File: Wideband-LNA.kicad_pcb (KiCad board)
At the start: 4 copper layers, 18.8 x 18.8 mm, 32 parts, among them J1 RF-IN, J2 RF-OUT, J3 USB_C_Receptacle_USB2.0_16P, U1 PGA-103, U2 AP2127K-ADJ

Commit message: After the fab and assy, components error fixes
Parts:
- added D2: 4v8, LED_SMD:LED_0402_1005Metric, F.Cu at (130.6, 95.4)
- added R10: 0, Resistor_SMD:R_0402_1005Metric, F.Cu at (110.6, 95.1)
- R1: value 10 -> 1K
- moved R1 10.9 mm to (121.4, 94.9)
- moved D1 1.36 mm to (116.9, 96.2)
- moved C9 0.36 mm to (117.1, 97.5)
- moved C3 0.13 mm to (112.9, 96.0)
- moved C1 0.12 mm to (112.9, 98.0)
- moved L2 0.11 mm to (112.9, 97.0)
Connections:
- R1 pad 2: Net-(C3-Pad1) -> Net-(D2-A)
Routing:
- net /5V: track 17.7 -> 19.3 mm
- net GND: track 15.7 -> 16.2 mm, vias 69 -> 68

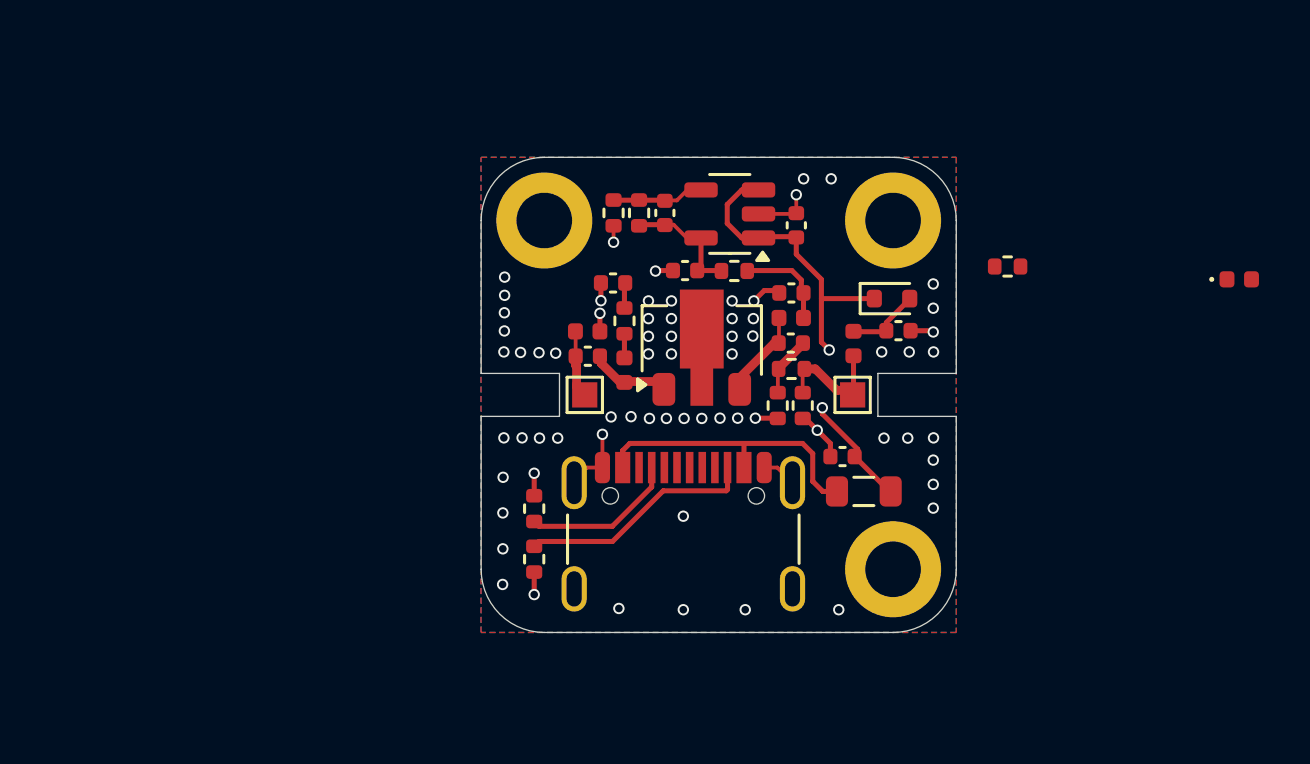
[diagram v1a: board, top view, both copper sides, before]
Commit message: Relayout for 25x25x50 extruded aluminum enclosure Axial coax connectors Isolation of LNA input and output Extensive shielding vias around RF traces
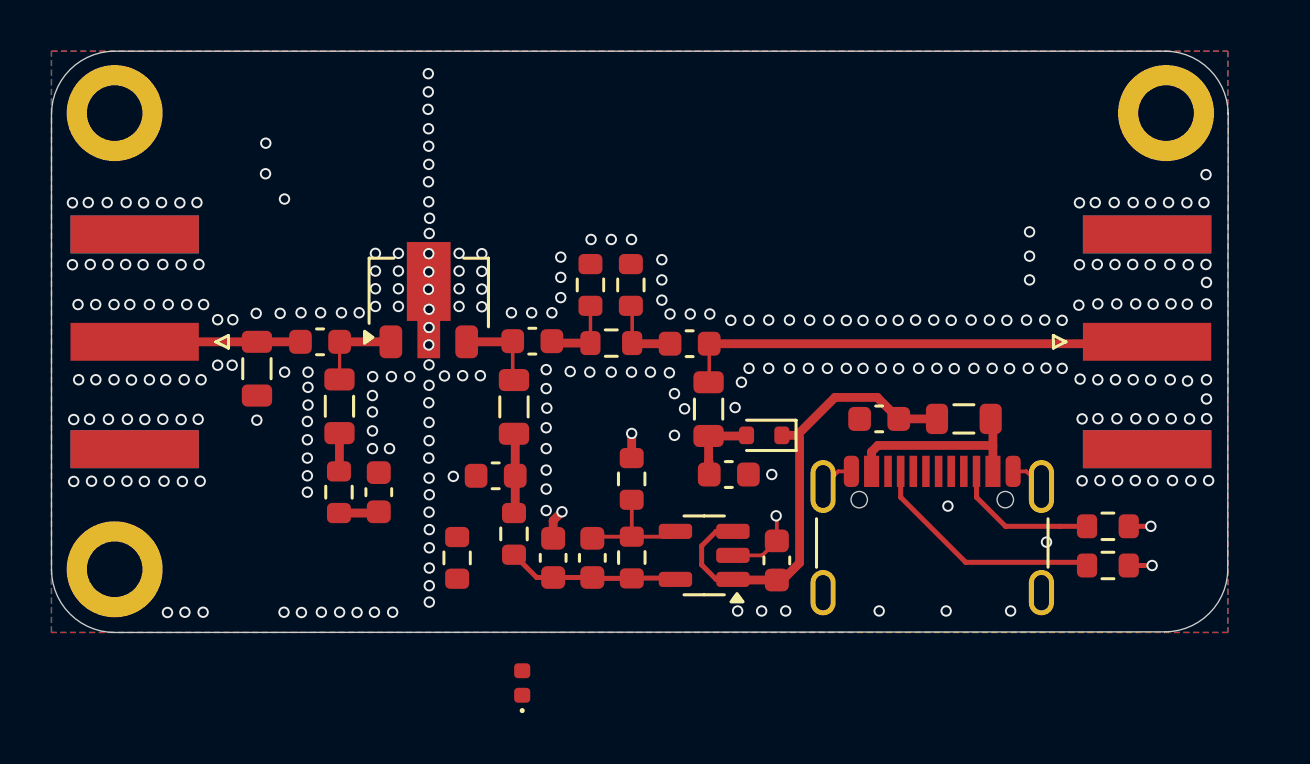
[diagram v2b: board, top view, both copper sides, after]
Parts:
- removed J1: RF-IN, TestPoint:TestPoint_Pad_1.0x1.0mm
- removed J2: RF-OUT, TestPoint:TestPoint_Pad_1.0x1.0mm
- added C10: 10n, Capacitor_SMD:C_0603_1608Metric, F.Cu at (108.8, 98.0)
- added J4: Conn_Coaxial, Connector_Coaxial:SMA_Amphenol_132289_EdgeMount, F.Cu at (127.0, 97.9)
- added J5: Conn_Coaxial, Connector_Coaxial:SMA_Amphenol_132289_EdgeMount, F.Cu at (86.9, 97.9)
- C1, C8: value 100n -> 10n; footprint Capacitor_SMD:C_0402_1005Metric -> Capacitor_SMD:C_0603_1608Metric
- C2, C3, C4, C5, C6, C7, C9: footprint Capacitor_SMD:C_0402_1005Metric -> Capacitor_SMD:C_0603_1608Metric
- L1, L2, L3, L4: footprint Inductor_SMD:L_0402_1005Metric -> Inductor_SMD:L_0805_2012Metric
- R1, R10, R2, R3, R4, R5, R6, R7, R8, R9: footprint Resistor_SMD:R_0402_1005Metric -> Resistor_SMD:R_0603_1608Metric
- moved D2 32.6 mm to (102.2, 111.4), turned to 90 degrees
- moved H3 30.8 mm to (86.1, 106.9)
- moved R1 24.6 mm to (99.7, 106.5), turned to -90 degrees
- moved R3 22.8 mm to (125.4, 106.8), turned to 0 degrees
- moved R4 22.7 mm to (125.4, 105.2), turned to 0 degrees
- moved H1 17.5 mm to (86.1, 88.8)
- moved C7 13.9 mm to (105.0, 106.5)
- moved C3 13.8 mm to (101.2, 103.2)
- moved R5 13.6 mm to (106.6, 106.4)
- moved R10 13.6 mm to (101.9, 105.5), turned to 90 degrees
- moved U2 13.5 mm to (109.4, 106.3)
- moved C6 13.3 mm to (112.3, 106.5)
- moved R9 13.2 mm to (95.0, 103.8), turned to -90 degrees
- moved L3 13.2 mm to (91.7, 99.0), turned to -90 degrees
- moved C4 12.5 mm to (103.5, 106.5), turned to 90 degrees
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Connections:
- L4 pad 2: Net-(J2-Pad1) -> Net-(J4-In)
- R7 pad 1: Net-(J2-Pad1) -> Net-(C10-Pad1)
- R8 pad 2: Net-(J2-Pad1) -> Net-(C10-Pad1)
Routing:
- net Net-(J4-In): track 0.00 -> 18.9 mm
- net GND: track 16.2 -> 9.72 mm, vias 68 -> 278
- net Net-(J2-Pad1): track 4.38 -> 0.00 mm
- net Net-(FB1-Pad1): track 11.6 -> 7.67 mm
- net Net-(J3-CC2): track 9.45 -> 5.88 mm
- net Net-(J3-CC1): track 6.14 -> 9.52 mm
- net Net-(C10-Pad1): track 0.00 -> 3.01 mm
- net Net-(J5-In): track 2.67 -> 5.37 mm
- net Net-(U2-ADJ): track 3.64 -> 4.86 mm
- net /4V8: track 5.89 -> 6.97 mm
- net Net-(C3-Pad1): track 3.93 -> 3.02 mm
- net Net-(C2-Pad1): track 1.00 -> 1.60 mm
- net Net-(C1-Pad2): track 2.42 -> 2.96 mm
- net Net-(C8-Pad2): track 3.19 -> 3.70 mm
- net /5V: track 19.3 -> 18.8 mm, vias 2 -> 0
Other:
- board size 18.8 x 18.8 mm -> 46.6 x 23 mm
- board text added: "PGA103 V4 LNA 28-1300 (C) wa1hco 2025 Creative Commons License V5 Attribute and Share Alike"
- board text removed: "PGA103 LNA 100-1300 (C) wa1hco 2025 Creative Commons License V5 Attribute and Share Alike"

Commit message: Branch for 2nd spin of V3 - move DC traces to layer 3 - leave layer 2 ground under component pads
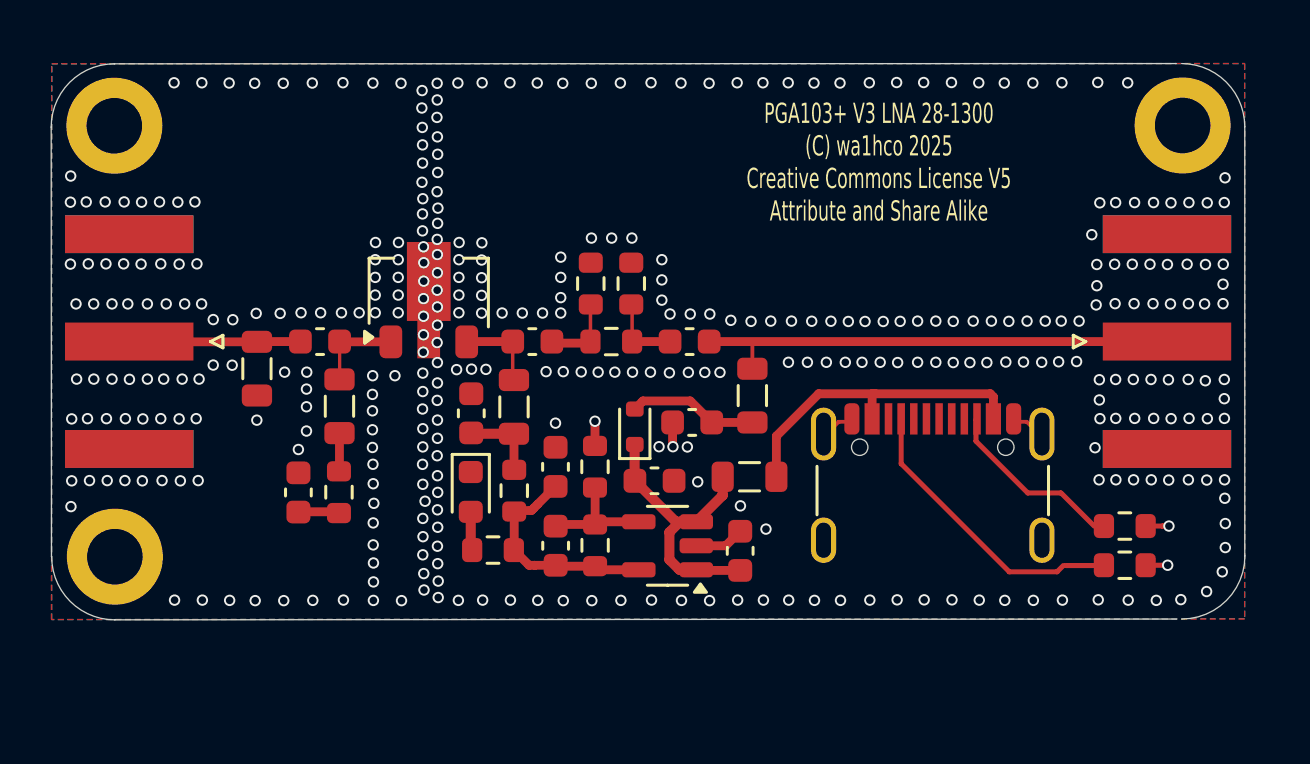
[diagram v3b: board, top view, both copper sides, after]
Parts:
- D2: footprint LED_SMD:LED_0402_1005Metric -> LED_SMD:LED_0603_1608Metric
- L1, L3: value 620n -> 680n
- U1: value PGA-103 -> PGA-103+
- moved C5 9.22 mm to (107.5, 103.4), turned to 0 degrees
- moved FB1 8.78 mm to (111.2, 103.2)
- moved D2 7.83 mm to (100.2, 103.8), turned to -90 degrees
- moved D1 5.13 mm to (106.7, 101.3), turned to 90 degrees
- moved C4 3.60 mm to (103.5, 102.8)
- moved C2 3.18 mm to (93.4, 103.9)
- moved C3 2.65 mm to (100.2, 100.7), turned to 90 degrees
- moved C9 2.52 mm to (109.0, 101.1), turned to 180 degrees
- moved J3 2.08 mm to (118.5, 104.7)
- moved L4 1.81 mm to (111.3, 100.0)
- moved R10 1.71 mm to (101.9, 103.8)
- moved C7 1.53 mm to (103.5, 106.0)
- moved R5 1.53 mm to (105.1, 106.0)
- moved R6 1.53 mm to (105.1, 102.8)
- moved C6 1.50 mm to (110.9, 106.2)
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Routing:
- net /5V: track 18.8 -> 12.0 mm
- net Net-(FB1-Pad1): track 7.67 -> 12.8 mm
- net /4V8: track 6.97 -> 9.28 mm
- net Net-(J3-CC1): track 9.52 -> 11.7 mm
- net Net-(D1-A): track 3.05 -> 5.14 mm
- net Net-(D2-A): track 0.00 -> 1.54 mm
- net Net-(J3-CC2): track 5.88 -> 7.26 mm
- net GND: track 9.72 -> 8.48 mm, vias 278 -> 366
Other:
- board size 46.6 x 23 mm -> 47.2 x 22 mm
- board text added: "PGA103+ V3 LNA 28-1300 (C) wa1hco 2025 Creative Commons License V5 Attribute and Share Alike"
- board text removed: "PGA103 V4 LNA 28-1300 (C) wa1hco 2025 Creative Commons License V5 Attribute and Share Alike"

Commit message: Removed cut outs under RF component pads Add stitching vias around all RF components Ensured two vias tied to ground planes for each RF component ground pads Improved layout to return ground currents closer to LNA and RF input/output path
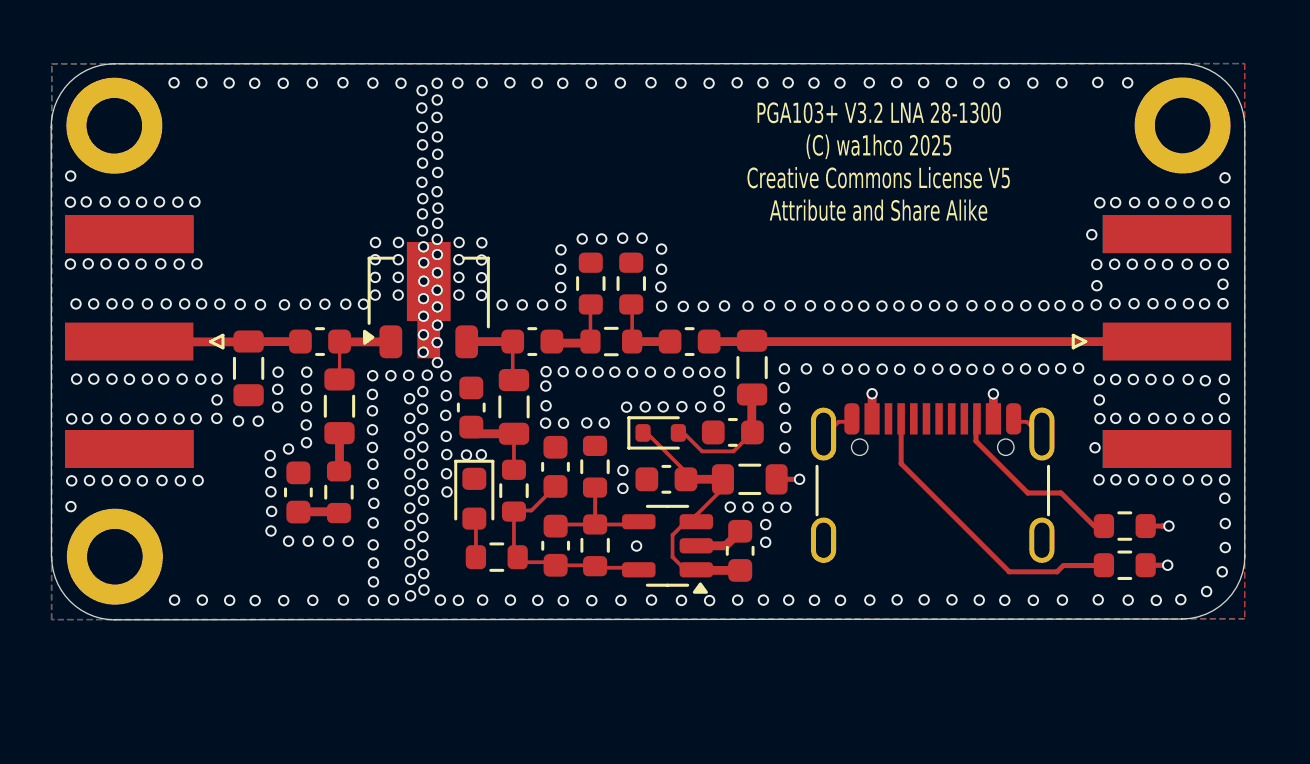
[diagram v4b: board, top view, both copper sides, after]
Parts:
- moved C9 1.66 mm to (110.6, 101.5)
- moved L4 1.11 mm to (111.3, 98.9)
- moved D1 1.05 mm to (107.7, 101.5), turned to 0 degrees
- moved C5 0.47 mm to (107.9, 103.3), turned to 180 degrees
- moved L3 0.33 mm to (91.4, 99.0)
- moved R1 0.32 mm to (101.2, 106.4)
- moved D2 0.30 mm to (100.3, 104.1)
- moved C3 0.23 mm to (100.2, 100.5)
- moved FB1 0.10 mm to (111.2, 103.3)
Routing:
- net GND: track 8.48 -> 6.54 mm, vias 366 -> 402
- net /5V: track 12.0 -> 11.1 mm
- net Net-(J4-In): track 19.2 -> 18.4 mm
- net Net-(FB1-Pad1): track 12.8 -> 13.4 mm, vias 0 -> 3
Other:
- outline, holes or cut-outs redrawn
- board text added: "PGA103+ V3.2 LNA 28-1300 (C) wa1hco 2025 Creative Commons License V5 Attribute and Share Alike"
- board text removed: "PGA103+ V3 LNA 28-1300 (C) wa1hco 2025 Creative Commons License V5 Attribute and Share Alike"

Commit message: Change from PGA103+ to TQP3M9036 for the 50x25x25 enclosure
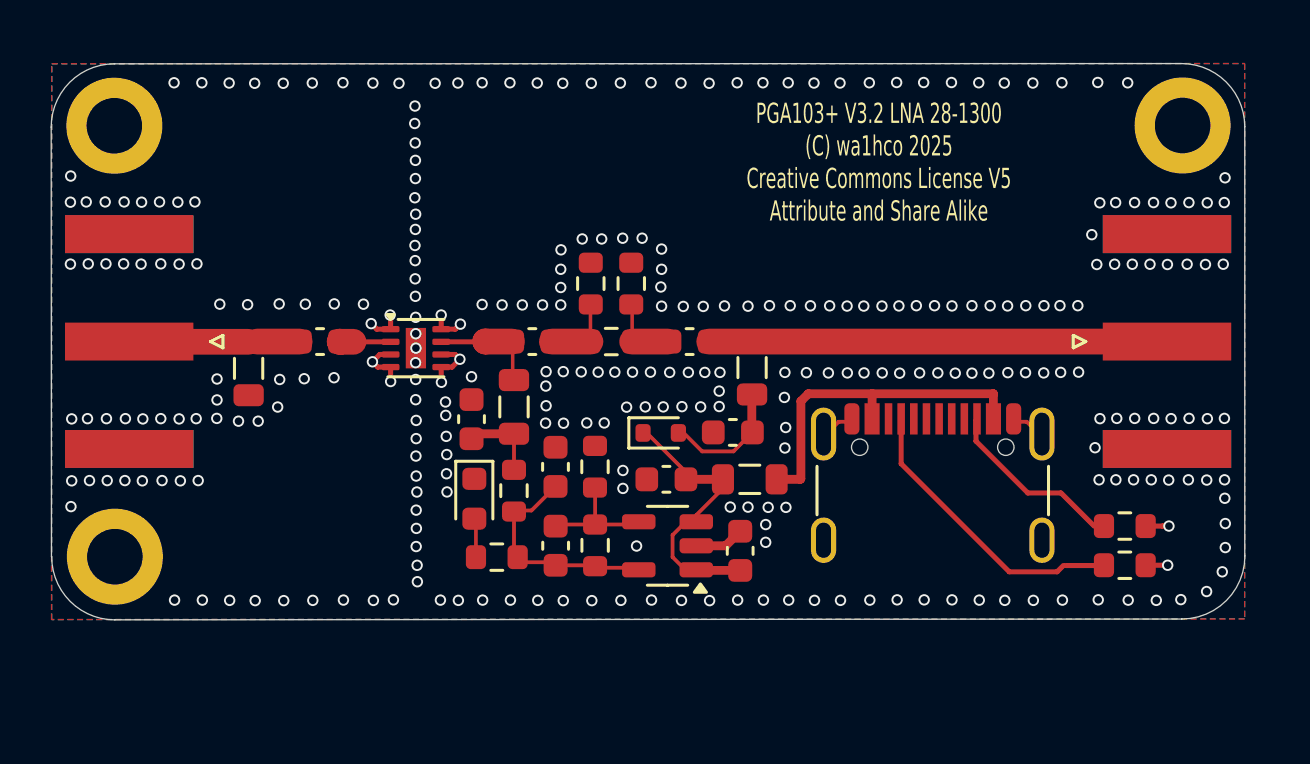
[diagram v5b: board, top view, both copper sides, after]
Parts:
- removed C2: 330p, Capacitor_SMD:C_0603_1608Metric
- removed L1: 680n, Inductor_SMD:L_0805_2012Metric
- removed R9: 150, Resistor_SMD:R_0603_1608Metric
- removed U1: PGA-103+, Package_TO_SOT_SMD:SOT-89-3
- added U3: TQP3M9036, Package_DFN_QFN:DFN-8-1EP_2x2mm_P0.5mm_EP0.8x1.6mm, F.Cu at (98.0, 98.2)
- moved C3 0.46 mm to (100.2, 101.0)
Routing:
- net GND: track 6.54 -> 13.9 mm, vias 402 -> 297
- net Net-(U3-RF_IN): track 3.70 -> 2.02 mm
- net Net-(C2-Pad1): track 1.66 -> 0.00 mm
- net Net-(L1-Pad2): track 1.33 -> 0.00 mm
- net Net-(U3-RF_OUT): track 3.19 -> 4.30 mm
- net Net-(FB1-Pad1): track 13.4 -> 13.8 mm, vias 3 -> 0
- removed copper zone on In1.Cu, net GND
- removed copper zone on In2.Cu, net GND
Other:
- copper layers 4 -> 2
